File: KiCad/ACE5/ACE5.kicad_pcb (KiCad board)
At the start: 2 copper layers, 160 x 100 mm, 99 parts, among them Q1 2N3904, Q3 BC237, U1 LM7805_TO220, X1 CRYSTALHC49U-V 6.556MHz, X2 5MHz

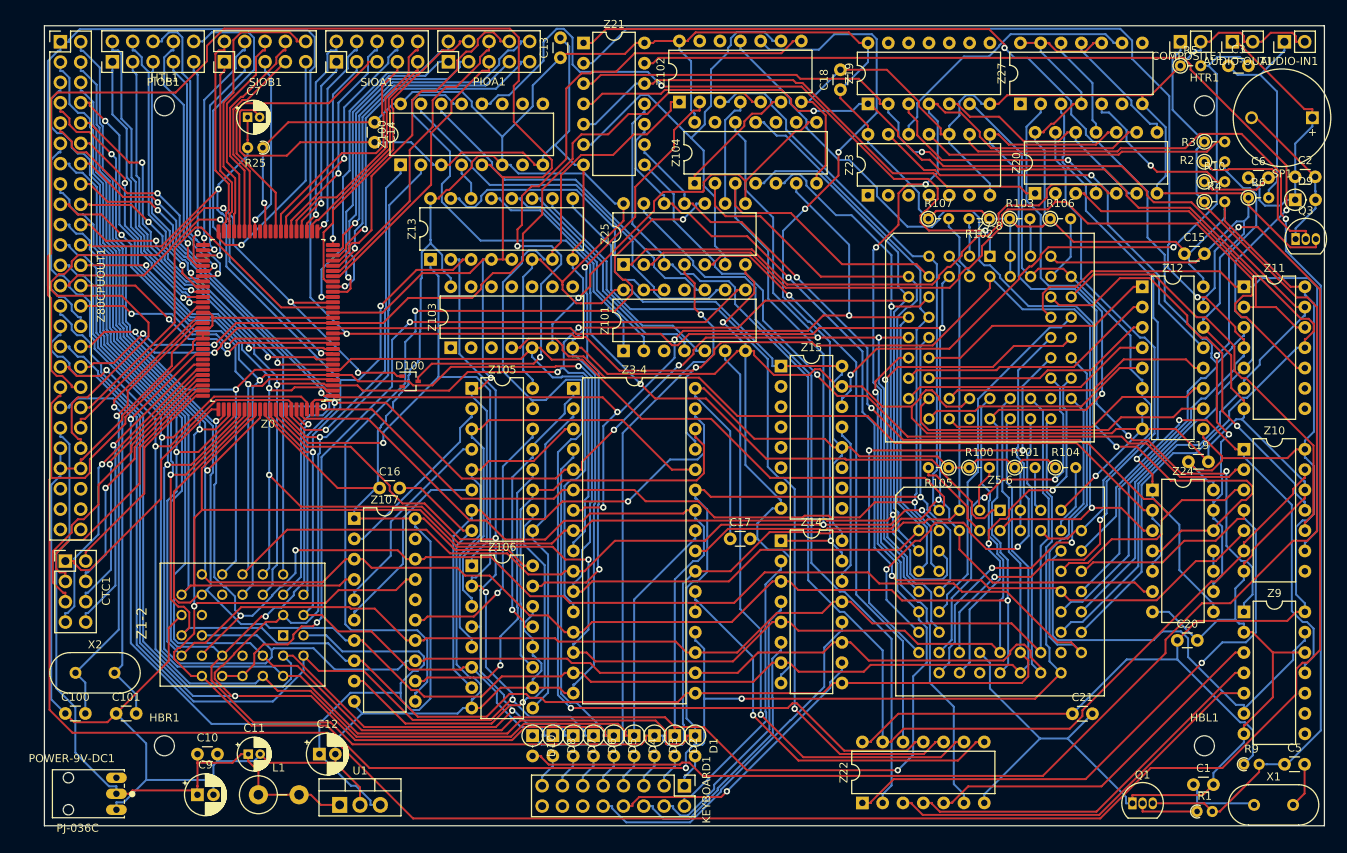
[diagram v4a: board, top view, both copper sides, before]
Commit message: Tidy add Zilog Logo.
Signed-off-by: John Bradley <flypie@rocketmail.com>
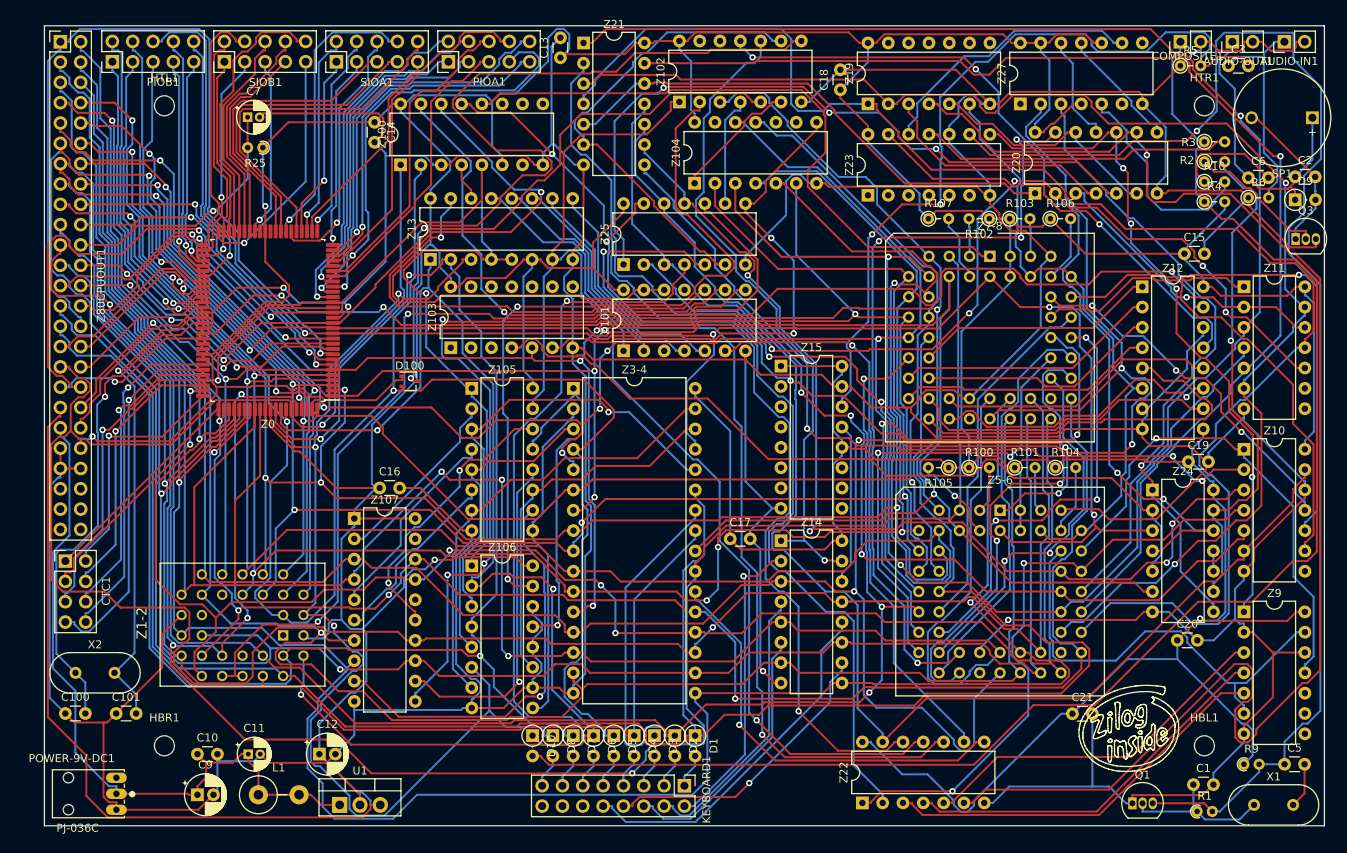
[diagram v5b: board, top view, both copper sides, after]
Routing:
- net #CPUCLK: track 315.3 -> 161.4 mm, vias 1 -> 4
- net /A8: track 263.0 -> 343.0 mm
- net /DA0: track 280.5 -> 348.2 mm, vias 3 -> 4
- net /VIDEN: track 126.9 -> 182.4 mm, vias 2 -> 1
- net /DA3: track 221.0 -> 271.3 mm, vias 1 -> 3
- net //MREQ: track 209.6 -> 165.1 mm, vias 1 -> 3
- net Net-(Z100-Pad14): track 44.3 -> 86.1 mm, vias 0 -> 1
- net /DA6: track 285.9 -> 253.4 mm
- net Net-(Z22-Pad12): track 74.8 -> 106.8 mm, vias 1 -> 2
- net #INT: track 100.2 -> 69.1 mm, vias 3 -> 1
- net +5V: track 866.0 -> 896.3 mm, vias 2 -> 3
- net Net-(C5-Pad1): track 141.3 -> 171.4 mm
- net /A15: track 154.4 -> 184.3 mm, vias 3 -> 4
- net /SCREENY4: track 159.1 -> 187.6 mm, vias 1 -> 0
- net GND: track 902.5 -> 925.4 mm, vias 2 -> 4
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
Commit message: Add Edge board to convert PINs to EDGECONNECTOR.
Signed-off-by: John Bradley <flypie@rocketmail.com>
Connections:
- Z80CPUOUT1 pad 1: //WR -> /#WE
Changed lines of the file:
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@@
     (zones 0)
     (modules 99)
-    (nets 264)
+    (nets 265)
   )
   (page A4)
@@
   (net 262 "Net-(R106-Pad2)")
   (net 263 "Net-(R107-Pad2)")
+  (net 264 /#WE)
   (net_class Default "This is the default net class."
     (clearance 0.1524)
@@
     (add_net +9V)
     (add_net /#PAGED8K)
+    (add_net /#WE)
     (add_net //BUSAK)
     (add_net //BUSRQ)
@@
       (net 25 /DA7))
     (pad 1 thru_hole rect (at 0 0) (size 1.7 1.7) (drill 1) (layers *.Cu *.Mask)
-      (net 18 //WR))
+      (net 264 /#WE))
     (model ${KISYS3DMOD}/Connector_PinHeader_2.54mm.3dshapes/PinHeader_2x25_P2.54mm_Vertical.wrl
       (at (xyz 0 0 0))

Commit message: Improve consitancy.
Signed-off-by: John Bradley <flypie@rocketmail.com>
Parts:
- added R32: 1K0, Resistor_THT:R_Axial_DIN0204_L3.6mm_D1.6mm_P2.54mm_Vertical, F.Cu at (32.0, 9.65)
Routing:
- net #CPUCLK: track 161.4 -> 285.1 mm, vias 4 -> 2
- net Net-(R32-Pad2): track 52.8 -> 150.7 mm, vias 1 -> 6
- net //HALT: track 45.2 -> 131.5 mm, vias 2 -> 1
- net /A6: track 223.0 -> 302.3 mm, vias 3 -> 8
- net //WR: track 267.2 -> 194.9 mm, vias 4 -> 6
- net //IOREQ: track 106.9 -> 170.1 mm, vias 2 -> 3
- net /DA6: track 253.4 -> 313.1 mm, vias 4 -> 3
- net //RD: track 219.5 -> 276.4 mm, vias 3 -> 6
- net Net-(Z102-Pad11): track 115.8 -> 170.3 mm, vias 4 -> 3
- net /DA0: track 348.2 -> 294.4 mm, vias 4 -> 7
- net /A1: track 243.6 -> 294.1 mm, vias 6 -> 8
- net +5V: track 896.3 -> 847.2 mm, vias 3 -> 5
- net /A15: track 184.3 -> 135.6 mm, vias 4 -> 5
- net Net-(Z5-6-Pad17): track 44.5 -> 90.5 mm, vias 0 -> 1
- net /DA5: track 230.9 -> 274.4 mm, vias 2 -> 5
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
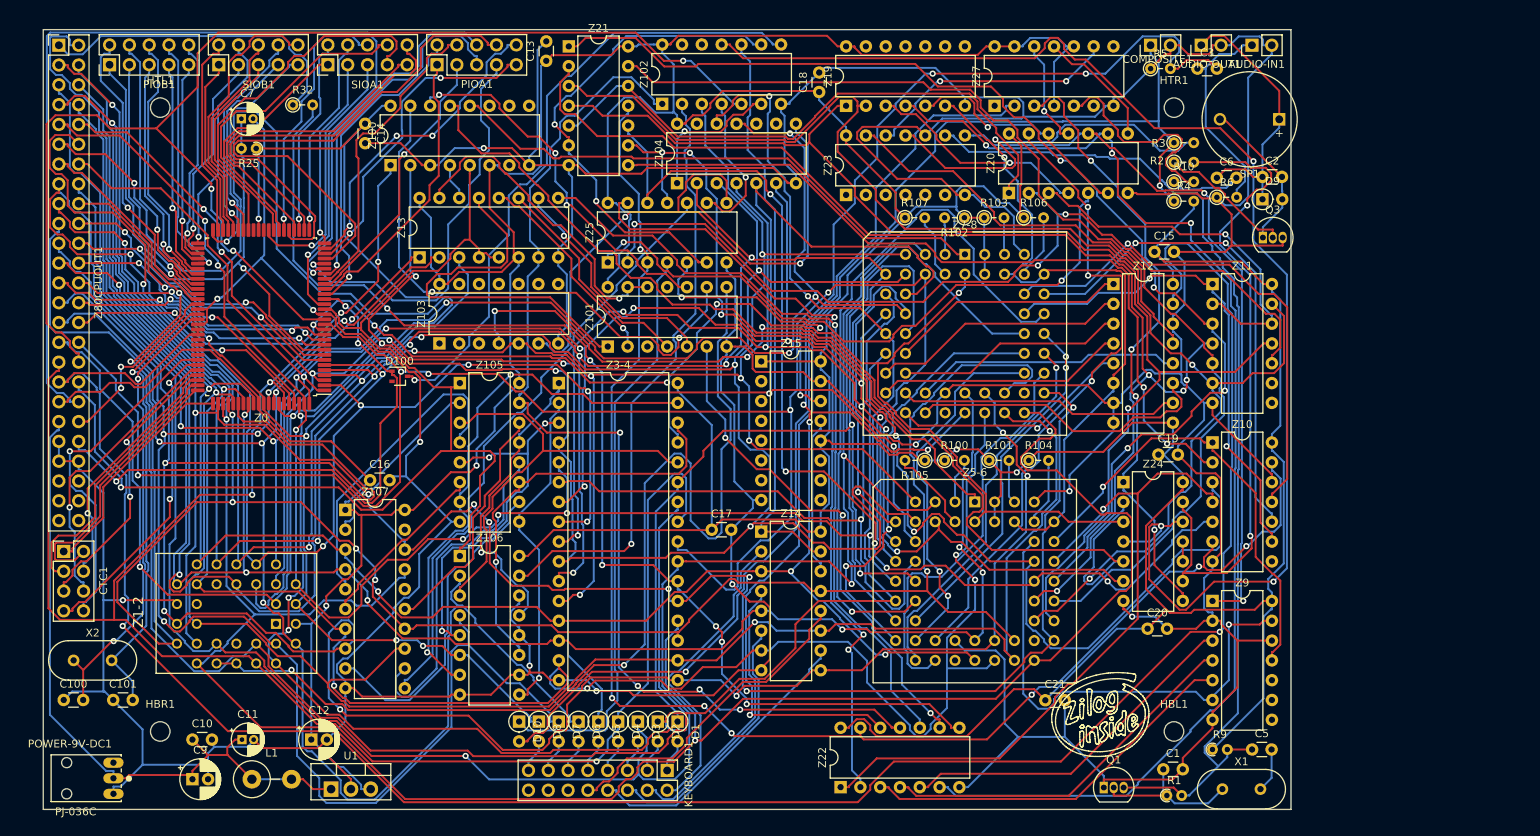
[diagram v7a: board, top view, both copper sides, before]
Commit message: Remove Speakrer leave 2 pin connector add single transistor amp to composite out.
Signed-off-by: John Bradley <flypie@rocketmail.com>
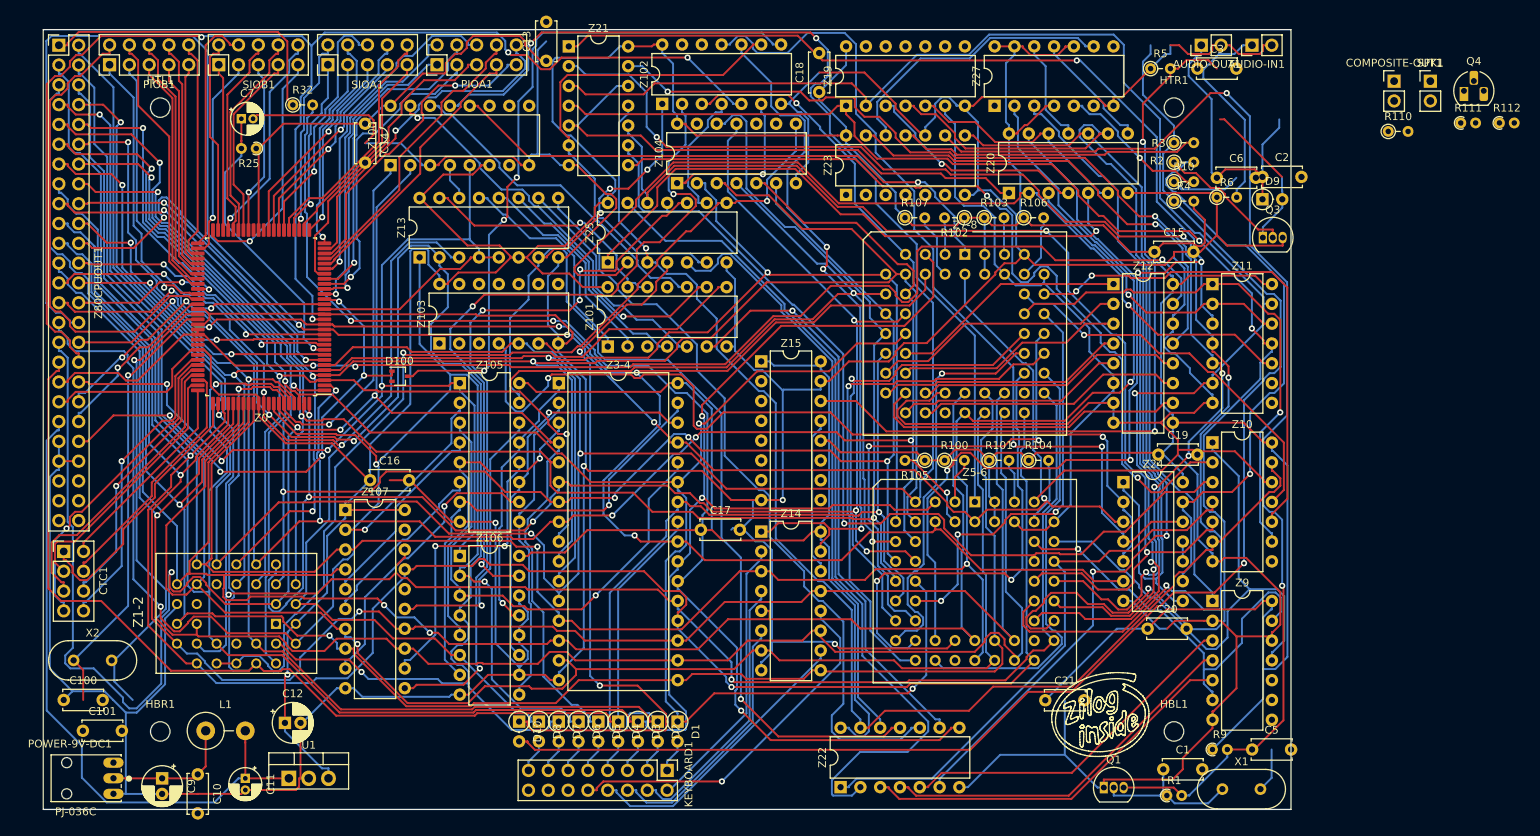
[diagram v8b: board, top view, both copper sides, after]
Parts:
- removed COMPOSITE1: Conn_01x02, Connector_PinHeader_2.54mm:PinHeader_1x02_P2.54mm_Vertical
- removed SP1: Speaker, Buzzer_Beeper:MagneticBuzzer_ProSignal_ABI-009-RC
- added COMPOSITE-OUT1: COMPOSITE-OUT1, Connector_PinHeader_2.54mm:PinHeader_1x02_P2.54mm_Vertical, F.Cu at (173.2, 6.60)
- added Q4: 2N3904, Package_TO_SOT_THT:TO-92L_HandSolder, F.Cu at (182.2, 7.85)
- added R110: 200, Resistor_THT:R_Axial_DIN0204_L3.6mm_D1.6mm_P2.54mm_Vertical, F.Cu at (172.5, 13.1)
- added R111: 100, Resistor_THT:R_Axial_DIN0204_L3.6mm_D1.6mm_P1.90mm_Vertical, F.Cu at (181.8, 12.0)
- added R112: 18, Resistor_THT:R_Axial_DIN0204_L3.6mm_D1.6mm_P1.90mm_Vertical, F.Cu at (186.7, 12.0)
- added SPK1: SPK1, Connector_PinHeader_2.54mm:PinHeader_1x02_P2.54mm_Vertical, F.Cu at (177.9, 6.60)
- C1, C10, C100, C101, C13, C14, C15, C16, C17, C18, C19, C2, C20, C21, C3, C5, C6: footprint Capacitor_THT:C_Disc_D3.0mm_W1.6mm_P2.50mm -> Capacitor_THT:C_Disc_D5.0mm_W2.5mm_P5.00mm
- R100, R101, R102, R103, R104, R105, R106, R107: value R -> 270
- moved L1 8.58 mm to (20.8, 89.9)
- moved U1 5.59 mm to (31.5, 96.0)
- moved C101 5.54 mm to (5.08, 89.9)
- moved C11 4.98 mm to (25.9, 96.0), turned to 270 degrees
- moved C10 4.51 mm to (19.8, 95.5), turned to 270 degrees
- moved C12 4.00 mm to (31.0, 88.9)
- moved C9 3.89 mm to (15.2, 96.0), turned to 270 degrees
- moved C17 1.40 mm to (84.3, 64.1)
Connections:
- C11 pad 1: +9V -> +9Vsm
- L1 pad 2: +9V -> +9Vsm
- U1 pad 1: +9V -> +9Vsm
- Z80CPUOUT1 pad 39: +9V -> +9Vsm
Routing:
- net #CPUCLK: track 285.1 -> 166.9 mm, vias 2 -> 3
- net //HALT: track 131.5 -> 38.1 mm, vias 1 -> 3
- net +9Vsm: track 0.00 -> 83.6 mm
- net /A8: track 342.5 -> 264.3 mm, vias 6 -> 4
- net +9V: track 88.2 -> 17.0 mm
- net /A6: track 302.3 -> 237.6 mm, vias 8 -> 7
- net //WR: track 194.9 -> 253.6 mm, vias 6 -> 4
- net /DA3: track 283.1 -> 225.8 mm, vias 6 -> 2
- net //RD: track 276.4 -> 219.1 mm, vias 6 -> 5
- net Net-(Z102-Pad11): track 170.3 -> 113.9 mm, vias 3 -> 2
- net /A1: track 294.1 -> 243.3 mm, vias 8 -> 4
- net /DA6: track 313.1 -> 262.7 mm, vias 3 -> 2
- net /DA5: track 274.4 -> 230.1 mm, vias 5 -> 2
- net /A9: track 285.5 -> 242.4 mm
- net /A2: track 286.3 -> 246.9 mm, vias 7 -> 4
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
